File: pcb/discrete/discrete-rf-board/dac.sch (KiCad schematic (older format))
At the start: 0 parts

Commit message: Design DAC/ADC stages, pass out all control signals to top sheet
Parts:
- added C? (x2): 1 uF, symbol Device:C_Small
- added C? (x2): 470 nF, symbol Device:C_Small
- added C? (x2): 100 nF, symbol Device:C_Small
- added C? (x2): 10 nF, symbol Device:C_Small
- added Q?: Q_NPN_BCE, symbol Device:Q_NPN_BCE
- added R?: 2kR, symbol Device:R_Small
- added R? (x3): 7.5kR 1%, symbol Device:R_Small
- added R? (x5): 15kR 1%, symbol Device:R_Small
- added R?: 470R, symbol Device:R_Small
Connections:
- new net: Q?.1 (B), R?.1, R?.2, R?.2
- new net: R?.1, R?.2, R?.2 (x3)
- new net +3V3: C?.1, C?.1, C?.1, C?.1, R?.1
- new net +5V: C?.1, C?.1, C?.1, C?.1, Q?.2 (C)
- new net D0: R?.1
- new net D1: R?.1
- new net D2: R?.1
- new net D3: R?.1
- new net DAC_GND: C?.2, C?.2, C?.2, C?.2, C?.2, C?.2, C?.2, C?.2, R?.2, R?.2
- new net OUT: Q?.3 (E), R?.1
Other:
- note added: "LSB"
- note added: "MSB"

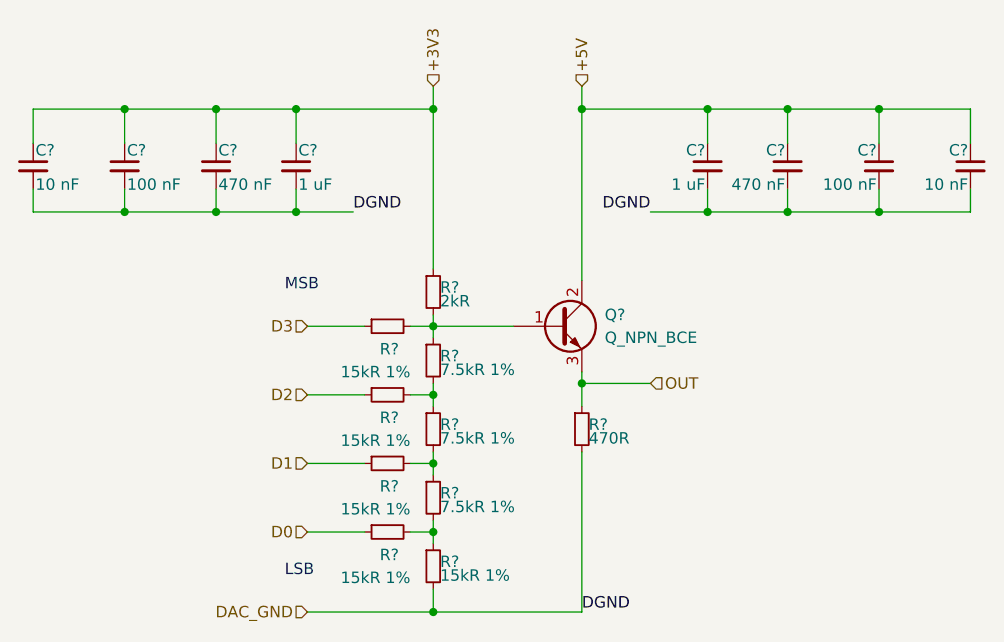
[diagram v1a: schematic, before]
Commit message: Wire out all control signals to connectors TODO PLL charge pump loop, bypass caps in attenuator circuit, antialiasing filter for ADC frontend
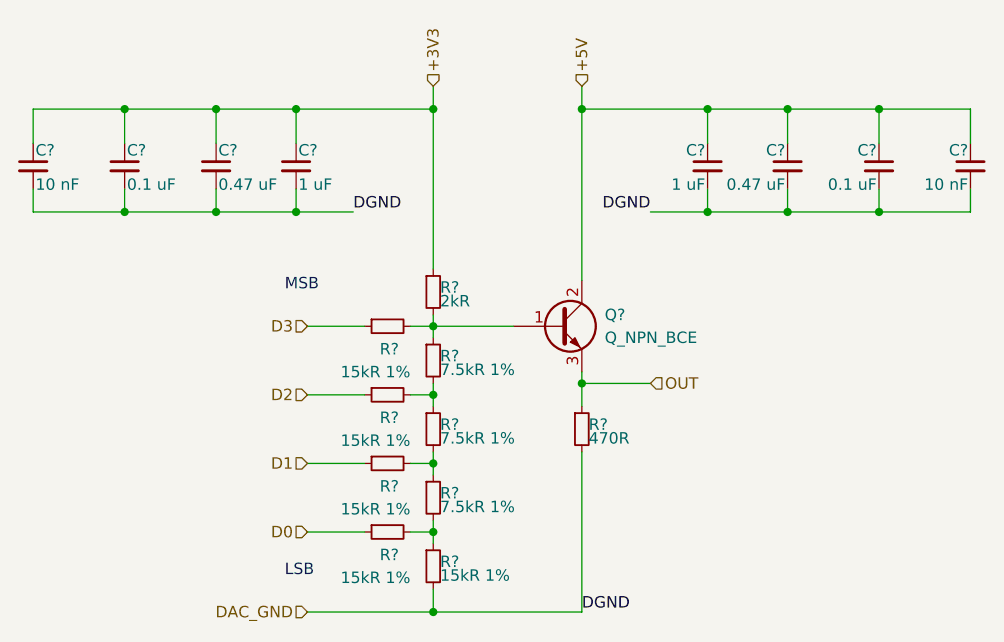
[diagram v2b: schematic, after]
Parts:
- C? (x2): value 470 nF -> 0.47 uF
- C? (x2): value 100 nF -> 0.1 uF
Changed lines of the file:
@@
 $Descr A4 11693 8268
 encoding utf-8
-Sheet 6 19
+Sheet 7 19
 Title ""
 Date ""
@@
 U 1 1 5DC04556
 P 2950 2150
+AR Path="/5CA6B0B3/5D83265A/5DC04556" Ref="C?"  Part="1"
+AR Path="/5CA6B0B3/5D9A8CAE/5DC04556" Ref="C?"  Part="1"
 F 0 "C?" H 2960 2220 50  0000 L CNN
 F 1 "1 uF" H 2960 2070 50  0000 L CNN
@@
 U 1 1 5DC04C84
 P 2600 2150
+AR Path="/5CA6B0B3/5D83265A/5DC04C84" Ref="C?"  Part="1"
+AR Path="/5CA6B0B3/5D9A8CAE/5DC04C84" Ref="C?"  Part="1"
 F 0 "C?" H 2610 2220 50  0000 L CNN
-F 1 "470 nF" H 2610 2070 50  0000 L CNN
+F 1 "0.47 uF" H 2610 2070 50  0000 L CNN
 F 2 "" H 2600 2150 50  0001 C CNN
 F 3 "~" H 2600 2150 50  0001 C CNN
@@
 U 1 1 5DC04F33
 P 2200 2150
+AR Path="/5CA6B0B3/5D83265A/5DC04F33" Ref="C?"  Part="1"
+AR Path="/5CA6B0B3/5D9A8CAE/5DC04F33" Ref="C?"  Part="1"
 F 0 "C?" H 2210 2220 50  0000 L CNN
-F 1 "100 nF" H 2210 2070 50  0000 L CNN
+F 1 "0.1 uF" H 2210 2070 50  0000 L CNN
 F 2 "" H 2200 2150 50  0001 C CNN
 F 3 "~" H 2200 2150 50  0001 C CNN
@@
 U 1 1 5DC05279
 P 1800 2150
+AR Path="/5CA6B0B3/5D83265A/5DC05279" Ref="C?"  Part="1"
+AR Path="/5CA6B0B3/5D9A8CAE/5DC05279" Ref="C?"  Part="1"
 F 0 "C?" H 1810 2220 50  0000 L CNN
 F 1 "10 nF" H 1810 2070 50  0000 L CNN
@@
 U 1 1 5DC0F871
 P 4750 2150
+AR Path="/5CA6B0B3/5D83265A/5DC0F871" Ref="C?"  Part="1"
+AR Path="/5CA6B0B3/5D9A8CAE/5DC0F871" Ref="C?"  Part="1"
 F 0 "C?" H 4760 2220 50  0000 L CNN
 F 1 "1 uF" H 4760 2070 50  0000 L CNN
@@
 U 1 1 5DC0F877
 P 5100 2150
+AR Path="/5CA6B0B3/5D83265A/5DC0F877" Ref="C?"  Part="1"
+AR Path="/5CA6B0B3/5D9A8CAE/5DC0F877" Ref="C?"  Part="1"
 F 0 "C?" H 5110 2220 50  0000 L CNN
-F 1 "470 nF" H 5110 2070 50  0000 L CNN
+F 1 "0.47 uF" H 5110 2070 50  0000 L CNN
 F 2 "" H 5100 2150 50  0001 C CNN
 F 3 "~" H 5100 2150 50  0001 C CNN
@@
 U 1 1 5DC0F87D
 P 5500 2150
+AR Path="/5CA6B0B3/5D83265A/5DC0F87D" Ref="C?"  Part="1"
+AR Path="/5CA6B0B3/5D9A8CAE/5DC0F87D" Ref="C?"  Part="1"
 F 0 "C?" H 5510 2220 50  0000 L CNN
-F 1 "100 nF" H 5510 2070 50  0000 L CNN
+F 1 "0.1 uF" H 5510 2070 50  0000 L CNN
 F 2 "" H 5500 2150 50  0001 C CNN
 F 3 "~" H 5500 2150 50  0001 C CNN
@@
 U 1 1 5DC0F883
 P 5900 2150
+AR Path="/5CA6B0B3/5D83265A/5DC0F883" Ref="C?"  Part="1"
+AR Path="/5CA6B0B3/5D9A8CAE/5DC0F883" Ref="C?"  Part="1"
 F 0 "C?" H 5910 2220 50  0000 L CNN
 F 1 "10 nF" H 5910 2070 50  0000 L CNN

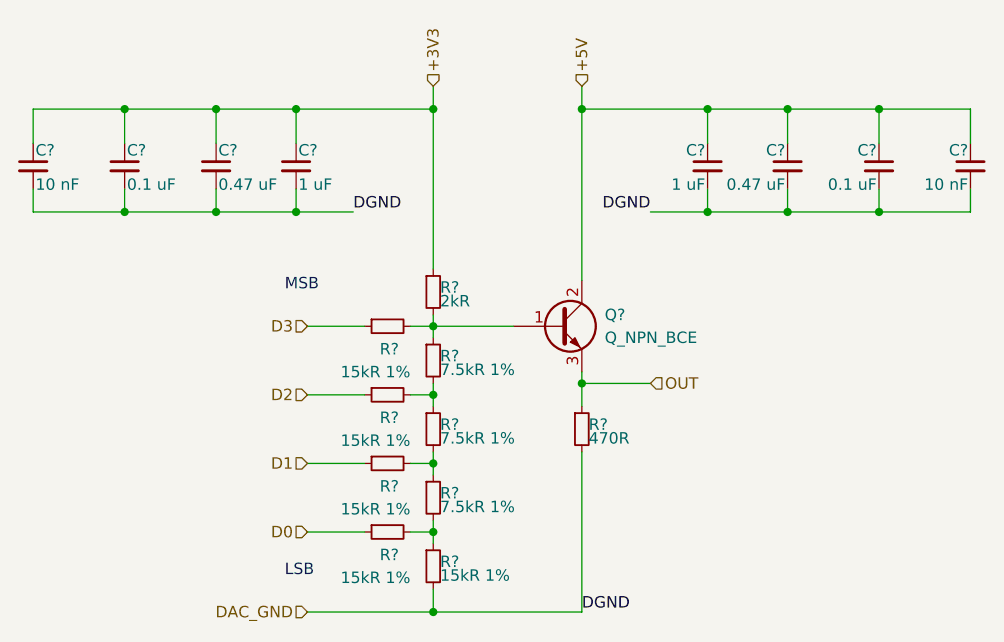
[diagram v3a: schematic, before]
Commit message: Add matching PNP/NPN transistor pairs, fix pin numbering for BFU520R transistors TODO fix biasing on power stage, source last NPN transistor, autofill and start sourcing passives
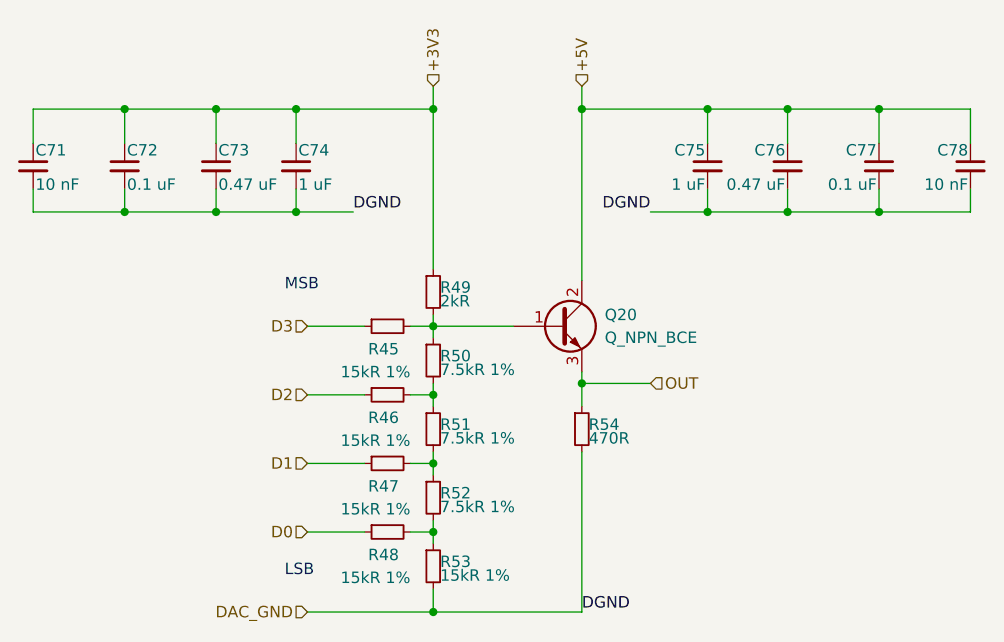
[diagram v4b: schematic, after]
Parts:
- gave numbers to parts that had none: 19
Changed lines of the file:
@@
 $EndDescr
 $Comp
-L Device:R_Small R?
+L Device:R_Small R49
 U 1 1 5D9928CB
 P 3550 2700
-AR Path="/5CA6B0B3/5D83265A/5D9928CB" Ref="R?"  Part="1"
-AR Path="/5CA6B0B3/5D9A8CAE/5D9928CB" Ref="R?"  Part="1"
-F 0 "R?" H 3580 2720 50  0000 L CNN
+AR Path="/5CA6B0B3/5D83265A/5D9928CB" Ref="R49"  Part="1"
+AR Path="/5CA6B0B3/5D9A8CAE/5D9928CB" Ref="R59"  Part="1"
+F 0 "R49" H 3580 2720 50  0000 L CNN
 F 1 "2kR" H 3580 2660 50  0000 L CNN
 F 2 "" H 3550 2700 50  0001 C CNN
@@
 $EndComp
 $Comp
-L Device:R_Small R?
+L Device:R_Small R50
 U 1 1 5D992BF1
 P 3550 3000
-AR Path="/5CA6B0B3/5D83265A/5D992BF1" Ref="R?"  Part="1"
-AR Path="/5CA6B0B3/5D9A8CAE/5D992BF1" Ref="R?"  Part="1"
-F 0 "R?" H 3580 3020 50  0000 L CNN
+AR Path="/5CA6B0B3/5D83265A/5D992BF1" Ref="R50"  Part="1"
+AR Path="/5CA6B0B3/5D9A8CAE/5D992BF1" Ref="R60"  Part="1"
+F 0 "R50" H 3580 3020 50  0000 L CNN
 F 1 "7.5kR 1%" H 3580 2960 50  0000 L CNN
 F 2 "" H 3550 3000 50  0001 C CNN
@@
 $EndComp
 $Comp
-L Device:R_Small R?
+L Device:R_Small R51
 U 1 1 5D9933B9
 P 3550 3300
-AR Path="/5CA6B0B3/5D83265A/5D9933B9" Ref="R?"  Part="1"
-AR Path="/5CA6B0B3/5D9A8CAE/5D9933B9" Ref="R?"  Part="1"
-F 0 "R?" H 3580 3320 50  0000 L CNN
+AR Path="/5CA6B0B3/5D83265A/5D9933B9" Ref="R51"  Part="1"
+AR Path="/5CA6B0B3/5D9A8CAE/5D9933B9" Ref="R61"  Part="1"
+F 0 "R51" H 3580 3320 50  0000 L CNN
 F 1 "7.5kR 1%" H 3580 3260 50  0000 L CNN
 F 2 "" H 3550 3300 50  0001 C CNN
@@
 $EndComp
 $Comp
-L Device:R_Small R?
+L Device:R_Small R52
 U 1 1 5D993558
 P 3550 3600
-AR Path="/5CA6B0B3/5D83265A/5D993558" Ref="R?"  Part="1"
-AR Path="/5CA6B0B3/5D9A8CAE/5D993558" Ref="R?"  Part="1"
-F 0 "R?" H 3580 3620 50  0000 L CNN
+AR Path="/5CA6B0B3/5D83265A/5D993558" Ref="R52"  Part="1"
+AR Path="/5CA6B0B3/5D9A8CAE/5D993558" Ref="R62"  Part="1"
+F 0 "R52" H 3580 3620 50  0000 L CNN
 F 1 "7.5kR 1%" H 3580 3560 50  0000 L CNN
 F 2 "" H 3550 3600 50  0001 C CNN
@@
 $EndComp
 $Comp
-L Device:R_Small R?
+L Device:R_Small R53
 U 1 1 5D993922
 P 3550 3900
-AR Path="/5CA6B0B3/5D83265A/5D993922" Ref="R?"  Part="1"
-AR Path="/5CA6B0B3/5D9A8CAE/5D993922" Ref="R?"  Part="1"
-F 0 "R?" H 3580 3920 50  0000 L CNN
+AR Path="/5CA6B0B3/5D83265A/5D993922" Ref="R53"  Part="1"
+AR Path="/5CA6B0B3/5D9A8CAE/5D993922" Ref="R63"  Part="1"
+F 0 "R53" H 3580 3920 50  0000 L CNN
 F 1 "15kR 1%" H 3580 3860 50  0000 L CNN
 F 2 "" H 3550 3900 50  0001 C CNN
@@
 $EndComp
 $Comp
-L Device:R_Small R?
+L Device:R_Small R45
 U 1 1 5D994F7A
 P 3350 2850
-AR Path="/5CA6B0B3/5D83265A/5D994F7A" Ref="R?"  Part="1"
-AR Path="/5CA6B0B3/5D9A8CAE/5D994F7A" Ref="R?"  Part="1"
-F 0 "R?" V 3450 2800 50  0000 L CNN
+AR Path="/5CA6B0B3/5D83265A/5D994F7A" Ref="R45"  Part="1"
+AR Path="/5CA6B0B3/5D9A8CAE/5D994F7A" Ref="R55"  Part="1"
+F 0 "R45" V 3450 2800 50  0000 L CNN
 F 1 "15kR 1%" V 3550 2750 50  0000 L CNN
 F 2 "" H 3350 2850 50  0001 C CNN
@@
 $EndComp
 $Comp
-L Device:R_Small R?
+L Device:R_Small R46
 U 1 1 5D996451
 P 3350 3150
-AR Path="/5CA6B0B3/5D83265A/5D996451" Ref="R?"  Part="1"
-AR Path="/5CA6B0B3/5D9A8CAE/5D996451" Ref="R?"  Part="1"
-F 0 "R?" V 3450 3100 50  0000 L CNN
+AR Path="/5CA6B0B3/5D83265A/5D996451" Ref="R46"  Part="1"
+AR Path="/5CA6B0B3/5D9A8CAE/5D996451" Ref="R56"  Part="1"
+F 0 "R46" V 3450 3100 50  0000 L CNN
 F 1 "15kR 1%" V 3550 3050 50  0000 L CNN
 F 2 "" H 3350 3150 50  0001 C CNN
@@
 $EndComp
 $Comp
-L Device:R_Small R?
+L Device:R_Small R47
 U 1 1 5D99666E
 P 3350 3450
-AR Path="/5CA6B0B3/5D83265A/5D99666E" Ref="R?"  Part="1"
-AR Path="/5CA6B0B3/5D9A8CAE/5D99666E" Ref="R?"  Part="1"
-F 0 "R?" V 3450 3400 50  0000 L CNN
+AR Path="/5CA6B0B3/5D83265A/5D99666E" Ref="R47"  Part="1"
+AR Path="/5CA6B0B3/5D9A8CAE/5D99666E" Ref="R57"  Part="1"
+F 0 "R47" V 3450 3400 50  0000 L CNN
 F 1 "15kR 1%" V 3550 3350 50  0000 L CNN
 F 2 "" H 3350 3450 50  0001 C CNN
@@
 $EndComp
 $Comp
-L Device:R_Small R?
+L Device:R_Small R48
 U 1 1 5D99690F
 P 3350 3750
-AR Path="/5CA6B0B3/5D83265A/5D99690F" Ref="R?"  Part="1"
-AR Path="/5CA6B0B3/5D9A8CAE/5D99690F" Ref="R?"  Part="1"
-F 0 "R?" V 3450 3700 50  0000 L CNN
+AR Path="/5CA6B0B3/5D83265A/5D99690F" Ref="R48"  Part="1"
+AR Path="/5CA6B0B3/5D9A8CAE/5D99690F" Ref="R58"  Part="1"
+F 0 "R48" V 3450 3700 50  0000 L CNN
 F 1 "15kR 1%" V 3550 3650 50  0000 L CNN
 F 2 "" H 3350 3750 50  0001 C CNN
@@
 	3550 3750 3550 3700
 $Comp
-L Device:Q_NPN_BCE Q?
+L Device:Q_NPN_BCE Q20
 U 1 1 5D998D16
 P 4100 2850
-AR Path="/5CA6B0B3/5D83265A/5D998D16" Ref="Q?"  Part="1"
-AR Path="/5CA6B0B3/5D9A8CAE/5D998D16" Ref="Q?"  Part="1"
-F 0 "Q?" H 4300 2900 50  0000 L CNN
+AR Path="/5CA6B0B3/5D83265A/5D998D16" Ref="Q20"  Part="1"
+AR Path="/5CA6B0B3/5D9A8CAE/5D998D16" Ref="Q21"  Part="1"
+F 0 "Q20" H 4300 2900 50  0000 L CNN
 F 1 "Q_NPN_BCE" H 4300 2800 50  0000 L CNN
 F 2 "" H 4300 2950 50  0001 C CNN
@@
 	3550 1800 3550 1900
 $Comp
-L Device:R_Small R?
+L Device:R_Small R54
 U 1 1 5D99E2FA
 P 4200 3300
-AR Path="/5CA6B0B3/5D83265A/5D99E2FA" Ref="R?"  Part="1"
-AR Path="/5CA6B0B3/5D9A8CAE/5D99E2FA" Ref="R?"  Part="1"
-F 0 "R?" H 4230 3320 50  0000 L CNN
+AR Path="/5CA6B0B3/5D83265A/5D99E2FA" Ref="R54"  Part="1"
+AR Path="/5CA6B0B3/5D9A8CAE/5D99E2FA" Ref="R64"  Part="1"
+F 0 "R54" H 4230 3320 50  0000 L CNN
 F 1 "470R" H 4230 3260 50  0000 L CNN
 F 2 "" H 4200 3300 50  0001 C CNN
@@
 Connection ~ 3550 4100
 $Comp
-L Device:C_Small C?
+L Device:C_Small C74
 U 1 1 5DC04556
 P 2950 2150
-AR Path="/5CA6B0B3/5D83265A/5DC04556" Ref="C?"  Part="1"
-AR Path="/5CA6B0B3/5D9A8CAE/5DC04556" Ref="C?"  Part="1"
-F 0 "C?" H 2960 2220 50  0000 L CNN
+AR Path="/5CA6B0B3/5D83265A/5DC04556" Ref="C74"  Part="1"
+AR Path="/5CA6B0B3/5D9A8CAE/5DC04556" Ref="C82"  Part="1"
+F 0 "C74" H 2960 2220 50  0000 L CNN
 F 1 "1 uF" H 2960 2070 50  0000 L CNN
 F 2 "" H 2950 2150 50  0001 C CNN
@@
 $EndComp
 $Comp
-L Device:C_Small C?
+L Device:C_Small C73
 U 1 1 5DC04C84
 P 2600 2150
-AR Path="/5CA6B0B3/5D83265A/5DC04C84" Ref="C?"  Part="1"
-AR Path="/5CA6B0B3/5D9A8CAE/5DC04C84" Ref="C?"  Part="1"
-F 0 "C?" H 2610 2220 50  0000 L CNN
+AR Path="/5CA6B0B3/5D83265A/5DC04C84" Ref="C73"  Part="1"
+AR Path="/5CA6B0B3/5D9A8CAE/5DC04C84" Ref="C81"  Part="1"
+F 0 "C73" H 2610 2220 50  0000 L CNN
 F 1 "0.47 uF" H 2610 2070 50  0000 L CNN
 F 2 "" H 2600 2150 50  0001 C CNN
@@
 $EndComp
 $Comp
-L Device:C_Small C?
+L Device:C_Small C72
 U 1 1 5DC04F33
 P 2200 2150
-AR Path="/5CA6B0B3/5D83265A/5DC04F33" Ref="C?"  Part="1"
-AR Path="/5CA6B0B3/5D9A8CAE/5DC04F33" Ref="C?"  Part="1"
-F 0 "C?" H 2210 2220 50  0000 L CNN
+AR Path="/5CA6B0B3/5D83265A/5DC04F33" Ref="C72"  Part="1"
+AR Path="/5CA6B0B3/5D9A8CAE/5DC04F33" Ref="C80"  Part="1"
+F 0 "C72" H 2210 2220 50  0000 L CNN
 F 1 "0.1 uF" H 2210 2070 50  0000 L CNN
 F 2 "" H 2200 2150 50  0001 C CNN
@@
 $EndComp
 $Comp
-L Device:C_Small C?
+L Device:C_Small C71
 U 1 1 5DC05279
 P 1800 2150
-AR Path="/5CA6B0B3/5D83265A/5DC05279" Ref="C?"  Part="1"
-AR Path="/5CA6B0B3/5D9A8CAE/5DC05279" Ref="C?"  Part="1"
-F 0 "C?" H 1810 2220 50  0000 L CNN
+AR Path="/5CA6B0B3/5D83265A/5DC05279" Ref="C71"  Part="1"
+AR Path="/5CA6B0B3/5D9A8CAE/5DC05279" Ref="C79"  Part="1"
+F 0 "C71" H 1810 2220 50  0000 L CNN
 F 1 "10 nF" H 1810 2070 50  0000 L CNN
 F 2 "" H 1800 2150 50  0001 C CNN
@@
 	2950 2350 2600 2350
 $Comp
-L Device:C_Small C?
+L Device:C_Small C75
 U 1 1 5DC0F871
 P 4750 2150
-AR Path="/5CA6B0B3/5D83265A/5DC0F871" Ref="C?"  Part="1"
-AR Path="/5CA6B0B3/5D9A8CAE/5DC0F871" Ref="C?"  Part="1"
-F 0 "C?" H 4760 2220 50  0000 L CNN
+AR Path="/5CA6B0B3/5D83265A/5DC0F871" Ref="C75"  Part="1"
+AR Path="/5CA6B0B3/5D9A8CAE/5DC0F871" Ref="C83"  Part="1"
+F 0 "C75" H 4760 2220 50  0000 L CNN
 F 1 "1 uF" H 4760 2070 50  0000 L CNN
 F 2 "" H 4750 2150 50  0001 C CNN
@@
 $EndComp
 $Comp
-L Device:C_Small C?
+L Device:C_Small C76
 U 1 1 5DC0F877
 P 5100 2150
-AR Path="/5CA6B0B3/5D83265A/5DC0F877" Ref="C?"  Part="1"
-AR Path="/5CA6B0B3/5D9A8CAE/5DC0F877" Ref="C?"  Part="1"
-F 0 "C?" H 5110 2220 50  0000 L CNN
+AR Path="/5CA6B0B3/5D83265A/5DC0F877" Ref="C76"  Part="1"
+AR Path="/5CA6B0B3/5D9A8CAE/5DC0F877" Ref="C84"  Part="1"
+F 0 "C76" H 5110 2220 50  0000 L CNN
 F 1 "0.47 uF" H 5110 2070 50  0000 L CNN
 F 2 "" H 5100 2150 50  0001 C CNN
@@
 $EndComp
 $Comp
-L Device:C_Small C?
+L Device:C_Small C77
 U 1 1 5DC0F87D
 P 5500 2150
-AR Path="/5CA6B0B3/5D83265A/5DC0F87D" Ref="C?"  Part="1"
-AR Path="/5CA6B0B3/5D9A8CAE/5DC0F87D" Ref="C?"  Part="1"
-F 0 "C?" H 5510 2220 50  0000 L CNN
+AR Path="/5CA6B0B3/5D83265A/5DC0F87D" Ref="C77"  Part="1"
+AR Path="/5CA6B0B3/5D9A8CAE/5DC0F87D" Ref="C85"  Part="1"
+F 0 "C77" H 5510 2220 50  0000 L CNN
 F 1 "0.1 uF" H 5510 2070 50  0000 L CNN
 F 2 "" H 5500 2150 50  0001 C CNN
@@
 $EndComp
 $Comp
-L Device:C_Small C?
+L Device:C_Small C78
 U 1 1 5DC0F883
 P 5900 2150
-AR Path="/5CA6B0B3/5D83265A/5DC0F883" Ref="C?"  Part="1"
-AR Path="/5CA6B0B3/5D9A8CAE/5DC0F883" Ref="C?"  Part="1"
-F 0 "C?" H 5910 2220 50  0000 L CNN
+AR Path="/5CA6B0B3/5D83265A/5DC0F883" Ref="C78"  Part="1"
+AR Path="/5CA6B0B3/5D9A8CAE/5DC0F883" Ref="C86"  Part="1"
+F 0 "C78" H 5910 2220 50  0000 L CNN
 F 1 "10 nF" H 5910 2070 50  0000 L CNN
 F 2 "" H 5900 2150 50  0001 C CNN
